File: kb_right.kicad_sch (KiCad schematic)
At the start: 181 parts, among them J1 10029449-001RLF, J2 Conn_02x06_Odd_Even, J3 Conn_02x06_Odd_Even, SW1 RotaryEncoder_Switch, SW2 RotaryEncoder

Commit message: added rgb end pinout
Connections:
- net +5V: no longer J2.5 (Pin_5)
- net RGB_R_END: now reaches D135.2 (DOUT)
- net RGB_R_END: now also J2.5 (Pin_5)
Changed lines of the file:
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@@
     (effects (font (size 1.27 1.27)) (justify left bottom))
   )
+  (label "RGB_R_END" (at 24.13 316.23 180)
+    (effects (font (size 1.27 1.27)) (justify right bottom))
+  )
   (label "COL0" (at 372.11 22.86 180)
     (effects (font (size 1.27 1.27)) (justify right bottom))
@@
     (effects (font (size 1.27 1.27)) (justify left bottom))
   )
+  (label "RGB_R_END" (at 384.81 81.28 180)
+    (effects (font (size 1.27 1.27)) (justify right bottom))
+  )
   (label "ROW5" (at 30.48 52.07 180)
     (effects (font (size 1.27 1.27)) (justify right bottom))
@@
     (pin "2")
   )
-  (symbol (lib_id "power:+5V") (at 384.81 81.28 90) (unit 1)
-    (in_bom yes) (on_board yes) (fields_autoplaced)
-    (property "Reference" "#PWR04" (id 0) (at 388.62 81.28 0)
-      (effects (font (size 1.27 1.27)) hide)
-    )
-    (property "Value" "+5V" (id 1) (at 381 81.2799 90)
-      (effects (font (size 1.27 1.27)) (justify left))
-    )
-    (property "Footprint" "" (id 2) (at 384.81 81.28 0)
-      (effects (font (size 1.27 1.27)) hide)
-    )
-    (property "Datasheet" "" (id 3) (at 384.81 81.28 0)
-      (effects (font (size 1.27 1.27)) hide)
-    )
-    (pin "1")
-  )
   (symbol (lib_id "MX_Alps_Hybrid:MX-NoLED") (at 106.68 34.29 0) (unit 1)
     (in_bom yes) (on_board yes) (fields_autoplaced)
@@
       (reference "#PWR03") (unit 1) (value "+5V") (footprint "")
     )
-    (path "/365b3093-ae3c-47a0-b1bd-53ada21b86ac"
-      (reference "#PWR04") (unit 1) (value "+5V") (footprint "")
-    )
     (path "/784ea5ef-81fc-4c69-a39e-addf5f61a67a"

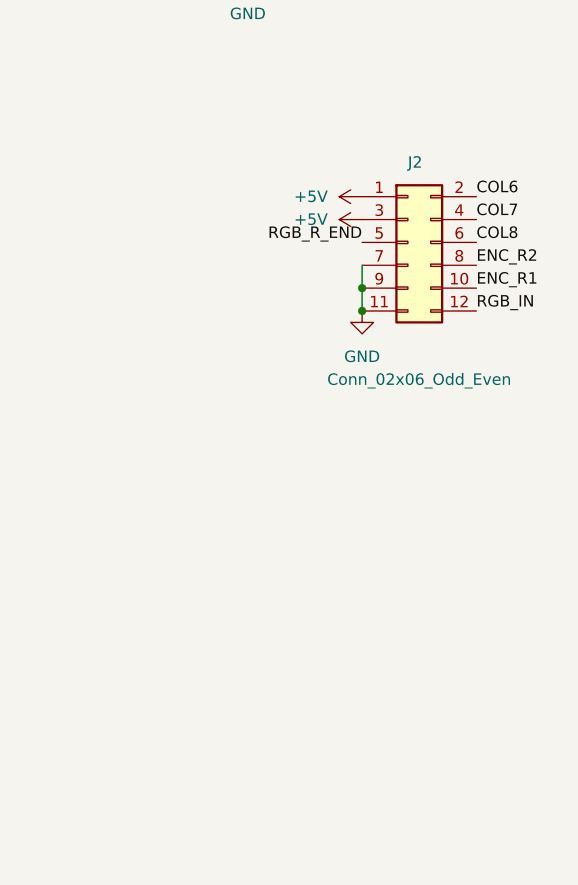
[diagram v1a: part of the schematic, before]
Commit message: changed pinout footprint
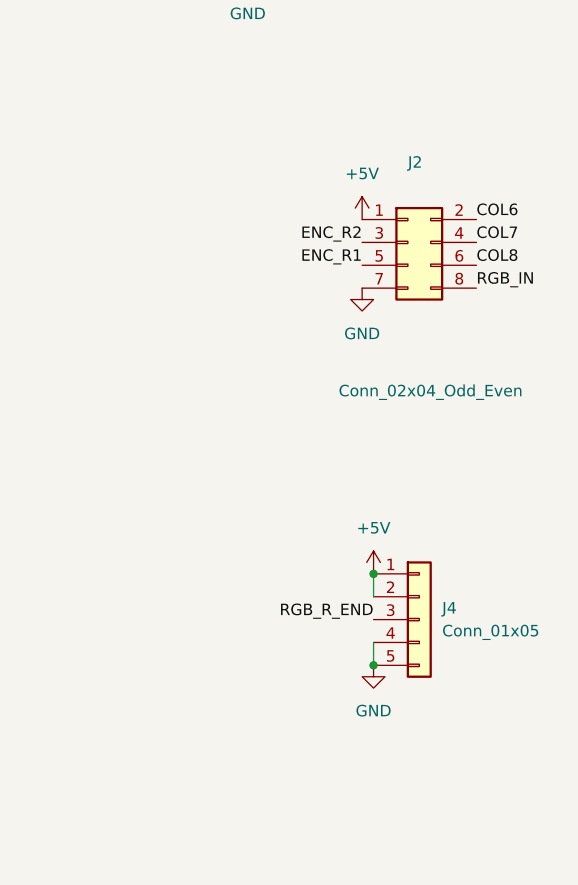
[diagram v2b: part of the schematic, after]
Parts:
- added J4: Conn_01x05, Connector_PinHeader_2.54mm:PinHeader_1x05_P2.54mm_Vertical, symbol Connector_Generic:Conn_01x05
- J2: value Conn_02x06_Odd_Even -> Conn_02x04_Odd_Even; footprint Connector_PinHeader_2.54mm:PinHeader_2x06_P2.54mm_Vertical -> Connector_PinHeader_2.54mm:PinHeader_2x04_P2.54mm_Vertical; symbol Connector_Generic:Conn_02x06_Odd_Even -> Connector_Generic:Conn_02x04_Odd_Even
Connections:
- net +5V: now also J4.1 (Pin_1), J4.2 (Pin_2); no longer J2.3 (Pin_3)
- net ENC_R1: now also J2.5 (Pin_5); no longer J2.10 (Pin_10)
- net ENC_R2: now also J2.3 (Pin_3); no longer J2.8 (Pin_8)
- net GND: now also J4.4 (Pin_4), J4.5 (Pin_5); no longer J2.11 (Pin_11), J2.9 (Pin_9)
- net RGB_IN: now also J2.8 (Pin_8); no longer J2.12 (Pin_12)
- net RGB_R_END: now also J4.3 (Pin_3); no longer J2.5 (Pin_5)

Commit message: before sending to jlc
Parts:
- J1: value 10029449-001RLF -> 10029449-111RLF
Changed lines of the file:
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@@
     (in_bom yes) (on_board yes) (fields_autoplaced)
     (property "Reference" "J1" (id 0) (at 384.81 15.24 0))
-    (property "Value" "10029449-001RLF" (id 1) (at 384.81 17.78 0))
+    (property "Value" "10029449-111RLF" (id 1) (at 384.81 17.78 0))
     (property "Footprint" "10029449-001RLF:AMPHENOL_10029449-001RLF" (id 2) (at 384.81 35.56 0)
       (effects (font (size 1.27 1.27)) (justify left bottom) hide)
@@
     )
     (path "/55604544-2b67-4b5c-bc42-fdfbb60d7ead"
-      (reference "J1") (unit 1) (value "10029449-001RLF") (footprint "10029449-001RLF:AMPHENOL_10029449-001RLF")
+      (reference "J1") (unit 1) (value "10029449-111RLF") (footprint "10029449-001RLF:AMPHENOL_10029449-001RLF")
     )
     (path "/b2538794-1fc7-407b-85ec-71f5ea4fc415"
